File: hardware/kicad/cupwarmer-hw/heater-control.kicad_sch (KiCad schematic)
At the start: 6 parts, among them Q1 AO3400 SOT-23

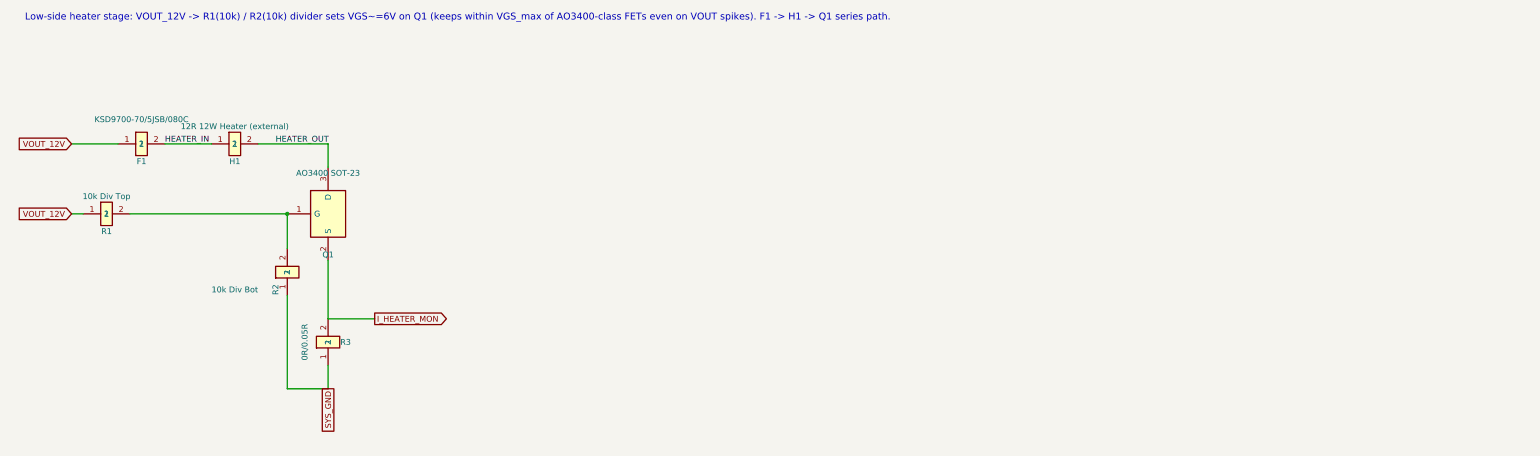
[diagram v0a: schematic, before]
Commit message: Add heater harness NTC routing
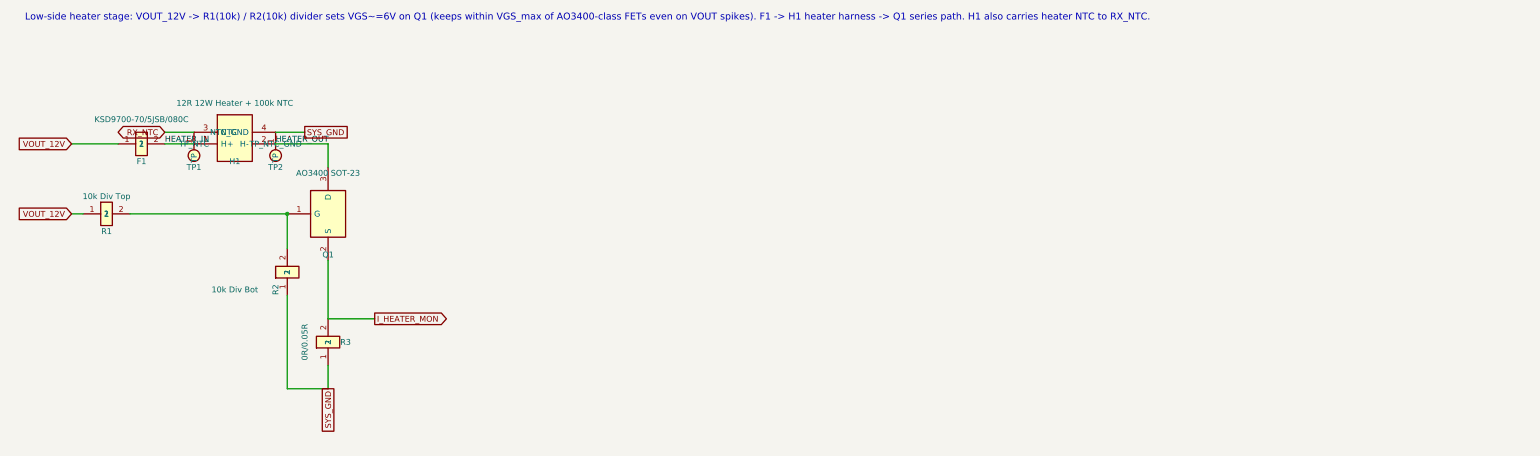
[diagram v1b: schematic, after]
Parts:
- added TP1: TP_NTC, cupwarmer:TestPoint_Pad_D1.0mm_NoSilk, symbol cupwarmer:TESTPAD_1
- added TP2: TP_NTC_GND, cupwarmer:TestPoint_Pad_D1.0mm_NoSilk, symbol cupwarmer:TESTPAD_1
- H1: value 12R 12W Heater (external) -> 12R 12W Heater + 100k NTC; footprint Connector_Wire:SolderWire-1sqmm_1x02_P5.4mm_D1.4mm_OD2.7mm -> cupwarmer:SolderWire-HeaterHarness_1x04_P5.0mm_D1.4mm; symbol cupwarmer:PASSIVE_2 -> cupwarmer:HEATER_HARNESS_4
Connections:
- net SYS_GND: now also H1.4 (NTC_GND), TP2.1 (TP)
- new net RX_NTC: H1.3 (NTC), TP1.1 (TP)
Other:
- note added: "Low-side heater stage: VOUT_12V -> R1(10k) / R2(10k) divider sets VGS~=6V on Q1 (keeps within VGS_max of AO3400-class FETs even on VOUT spikes). F1 -> H1 heater harness -> Q1 series path. H1 also carries heater NTC to RX_NTC."
- note removed: "Low-side heater stage: VOUT_12V -> R1(10k) / R2(10k) divider sets VGS~=6V on Q1 (keeps within VGS_max of AO3400-class FETs even on VOUT spikes). F1 -> H1 -> Q1 series path."
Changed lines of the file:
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@@
 		(comment 2 "Initial functional draft")
 	)
-	(text "Low-side heater stage: VOUT_12V -> R1(10k) / R2(10k) divider sets VGS~=6V on Q1 (keeps within VGS_max of AO3400-class FETs even on VOUT spikes). F1 -> H1 -> Q1 series path."
+	(text "Low-side heater stage: VOUT_12V -> R1(10k) / R2(10k) divider sets VGS~=6V on Q1 (keeps within VGS_max of AO3400-class FETs even on VOUT spikes). F1 -> H1 heater harness -> Q1 series path. H1 also carries heater NTC to RX_NTC."
 		(exclude_from_sim no)
 		(at 30.48 31.75 0)
@@
 	(wire
 		(pts
-			(xy 60.96 58.42) (xy 71.12 58.42)
-		)
-		(stroke
-			(width 0)
-			(type solid)
-		)
-	)
-	(wire
-		(pts
-			(xy 81.28 58.42) (xy 96.52 58.42)
+			(xy 60.96 58.42) (xy 67.31 58.42)
+		)
+		(stroke
+			(width 0)
+			(type solid)
+		)
+	)
+	(wire
+		(pts
+			(xy 85.09 58.42) (xy 96.52 58.42)
 		)
 		(stroke
@@
 		(pts
 			(xy 96.52 58.42) (xy 96.52 63.5)
+		)
+		(stroke
+			(width 0)
+			(type solid)
+		)
+	)
+	(wire
+		(pts
+			(xy 60.96 55.88) (xy 67.31 55.88)
+		)
+		(stroke
+			(width 0)
+			(type solid)
+		)
+	)
+	(wire
+		(pts
+			(xy 85.09 55.88) (xy 91.44 55.88)
 		)
 		(stroke
@@
 		(property "Intersheetrefs" "${INTERSHEET_REFS}"
 			(at 106.68 96.52 0)
+			(hide yes)
+			(show_name no)
+			(do_not_autoplace no)
+			(effects
+				(font
+					(size 1.27 1.27)
+				)
+			)
+		)
+	)
+	(global_label "RX_NTC"
+		(shape bidirectional)
+		(at 60.96 55.88 180)
+		(effects
+			(font
+				(size 1.27 1.27)
+			)
+			(justify right)
+		)
+		(property "Intersheetrefs" "${INTERSHEET_REFS}"
+			(at 60.96 55.88 0)
+			(hide yes)
+			(show_name no)
+			(do_not_autoplace no)
+			(effects
+				(font
+					(size 1.27 1.27)
+				)
+			)
+		)
+	)
+	(global_label "SYS_GND"
+		(shape passive)
+		(at 91.44 55.88 0)
+		(effects
+			(font
+				(size 1.27 1.27)
+			)
+			(justify left)
+		)
+		(property "Intersheetrefs" "${INTERSHEET_REFS}"
+			(at 91.44 55.88 0)
 			(hide yes)
 			(show_name no)
@@
 	)
 	(symbol
-		(lib_id "cupwarmer:PASSIVE_2")
-		(at 76.2 58.42 0)
+		(lib_id "cupwarmer:HEATER_HARNESS_4")
+		(at 76.2 57.15 0)
 		(unit 1)
 		(body_style 1)
@@
 			)
 		)
-		(property "Value" "12R 12W Heater (external)"
-			(at 76.2 54.61 0)
-			(show_name no)
-			(do_not_autoplace no)
-			(effects
-				(font
-					(size 1.27 1.27)
-				)
-			)
-		)
-		(property "Footprint" "Connector_Wire:SolderWire-1sqmm_1x02_P5.4mm_D1.4mm_OD2.7mm"
-			(at 76.2 58.42 0)
+		(property "Value" "12R 12W Heater + 100k NTC"
+			(at 76.2 49.53 0)
+			(show_name no)
+			(do_not_autoplace no)
+			(effects
+				(font
+					(size 1.27 1.27)
+				)
+			)
+		)
+		(property "Footprint" "cupwarmer:SolderWire-HeaterHarness_1x04_P5.0mm_D1.4mm"
+			(at 76.2 57.15 0)
 			(hide yes)
 			(show_name no)
@@
 		)
 		(property "Datasheet" "~"
-			(at 76.2 58.42 0)
-			(hide yes)
-			(show_name no)
-			(do_not_autoplace no)
-			(effects
-				(font
-					(size 1.27 1.27)
-				)
-			)
-		)
-		(property "Description" "Heater element after thermal cutoff; series path continues to Q1"
-			(at 76.2 58.42 0)
+			(at 76.2 57.15 0)
+			(hide yes)
+			(show_name no)
+			(do_not_autoplace no)
+			(effects
+				(font
+					(size 1.27 1.27)
+				)
+			)
+		)
+		(property "Description" "Four-wire silicone heater harness: H+ after F1, H- to Q1 drain, embedded 100k NTC to RX_NTC/SYS_GND"
+			(at 76.2 57.15 0)
 			(hide yes)
 			(show_name no)
@@
 		)
 		(pin "2"
+		)
+		(pin "3"
+		)
+		(pin "4"
 		)
 		(instances
@@
 					(unit 1)
 				)
+			)
+		)
+	)
+	(symbol
+		(lib_id "cupwarmer:TESTPAD_1")
+		(at 67.31 60.96 0)
+		(unit 1)
+		(body_style 1)
+		(exclude_from_sim no)
+		(in_bom no)
+		(on_board yes)
+		(in_pos_files no)
+		(dnp no)
+		(property "Reference" "TP1"
+			(at 67.31 63.5 0)
+			(show_name no)
+			(do_not_autoplace no)
+			(effects
+				(font
+					(size 1.27 1.27)
+				)
+			)
+		)
+		(property "Value" "TP_NTC"
+			(at 67.31 58.42 0)
+			(show_name no)
+			(do_not_autoplace no)
+			(effects
+				(font
+					(size 1.27 1.27)
+				)
+			)
+		)
+		(property "Footprint" "cupwarmer:TestPoint_Pad_D1.0mm_NoSilk"
+			(at 67.31 60.96 0)
+			(hide yes)
+			(show_name no)
+			(do_not_autoplace no)
+			(effects
+				(font
+					(size 1.27 1.27)
+				)
+			)
+		)
+		(property "Datasheet" "~"
+			(at 67.31 60.96 0)
+			(hide yes)
+			(show_name no)
+			(do_not_autoplace no)
+			(effects
+				(font
+					(size 1.27 1.27)
+				)
+			)
+		)
+		(property "Description" "DMM probe pad for heater NTC before powered test"
+			(at 67.31 60.96 0)
+			(hide yes)
+			(show_name no)
+			(do_not_autoplace no)
+			(effects
+				(font
+					(size 1.27 1.27)
+				)
+			)
+		)
+		(pin "1"
+		)
+		(instances
+			(project "cupwarmer-hw"
+				(path "/f3c63676-f392-4700-9f58-a6787e1eb284/22222222-2222-2222-2222-222222222222"
+					(reference "TP1")
+					(unit 1)
+				)
+			)
+		)
+	)
+	(symbol
+		(lib_id "cupwarmer:TESTPAD_1")
+		(at 85.09 60.96 0)
+		(unit 1)
+		(body_style 1)
+		(exclude_from_sim no)
+		(in_bom no)
+		(on_board yes)
+		(in_pos_files no)
+		(dnp no)
+		(property "Reference" "TP2"
+			(at 85.09 63.5 0)
+			(show_name no)
+			(do_not_autoplace no)
+			(effects
+				(font
+					(size 1.27 1.27)
+				)
+			)
+		)
+		(property "Value" "TP_NTC_GND"
+			(at 85.09 58.42 0)
+			(show_name no)
+			(do_not_autoplace no)
+			(effects
+				(font
+					(size 1.27 1.27)
+				)
+			)
+		)
+		(property "Footprint" "cupwarmer:TestPoint_Pad_D1.0mm_NoSilk"
+			(at 85.09 60.96 0)
+			(hide yes)
+			(show_name no)
+			(do_not_autoplace no)
+			(effects
+				(font
+					(size 1.27 1.27)
+				)
+			)
+		)
+		(property "Datasheet" "~"
+			(at 85.09 60.96 0)
+			(hide yes)
+			(show_name no)
+			(do_not_autoplace no)
+			(effects
+				(font
+					(size 1.27 1.27)
+				)
+			)
+		)
+		(property "Description" "DMM return pad for heater NTC before powered test"
+			(at 85.09 60.96 0)
+			(hide yes)
+			(show_name no)
+			(do_not_autoplace no)
+			(effects
+				(font
+					(size 1.27 1.27)
+				)
+			)
+		)
+		(pin "1"
+		)
+		(instances
+			(project "cupwarmer-hw"
+				(path "/f3c63676-f392-4700-9f58-a6787e1eb284/22222222-2222-2222-2222-222222222222"
+					(reference "TP2")
+					(unit 1)
+				)
